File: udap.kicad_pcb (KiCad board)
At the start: 2 copper layers, 25 x 10 mm, 25 parts, among them J201 Conn_02x04_Counter_Clockwise, P1 USB_C_Plug, U2 MIC5245-3.3YM5, U201 NUF6401MNT1, U202 STM32F042F6Px, U4 NUF2042XV6T1G

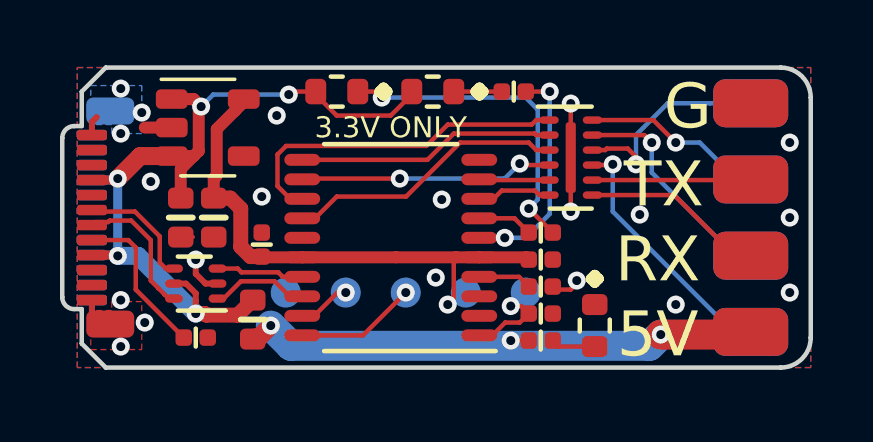
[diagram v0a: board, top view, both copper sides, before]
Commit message: Move the testpoints towards the USB connector
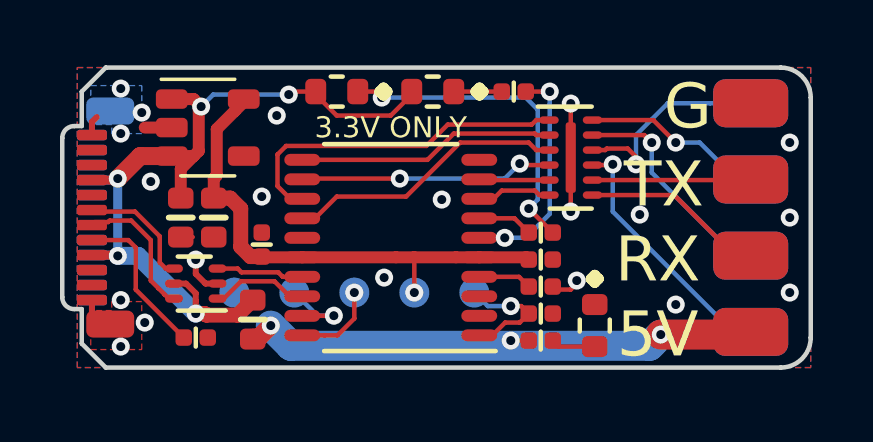
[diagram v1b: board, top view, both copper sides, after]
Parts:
- moved TP1 1.71 mm to (97.3, 108.5)
- moved TP2 1.71 mm to (99.3, 108.5)
- moved TP201 1.71 mm to (101.3, 108.5)
- moved TP202 1.71 mm to (103.3, 108.5)
- moved TP3 1.71 mm to (95.3, 108.5)
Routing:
- net /core/SWDIO: track 1.77 -> 3.09 mm
- net /core/SWCLK: track 4.04 -> 2.83 mm
- net +3V3: track 18.2 -> 17.0 mm
- net /core/BOOT0: track 3.77 -> 4.53 mm
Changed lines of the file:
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@@
     (thickness 0.7)
     (drawings 30)
-    (tracks 262)
+    (tracks 265)
     (zones 0)
     (modules 25)
@@
   (setup
     (last_trace_width 0.15)
+    (user_trace_width 0.15)
+    (user_trace_width 0.6)
     (trace_clearance 0.15)
     (zone_clearance 0.15)
@@
   )
   (module TestPoint:TestPoint_Pad_D1.0mm (layer B.Cu)
-    (at 105 108.5)
+    (at 103.2855 108.5)
     (descr "SMD pad as test Point, diameter 1.0mm")
     (tags "test point SMD pad")
@@
   )
   (module TestPoint:TestPoint_Pad_D1.0mm (layer B.Cu)
-    (at 103 108.5)
+    (at 101.2855 108.5)
     (descr "SMD pad as test Point, diameter 1.0mm")
     (tags "test point SMD pad")
@@
   )
   (module TestPoint:TestPoint_Pad_D1.0mm (layer B.Cu)
-    (at 97 108.5)
+    (at 95.2855 108.5)
     (descr "SMD pad as test Point, diameter 1.0mm")
     (tags "test point SMD pad")
@@
   )
   (module TestPoint:TestPoint_Pad_D1.0mm (layer B.Cu)
-    (at 101 108.5)
+    (at 99.2855 108.5)
     (descr "SMD pad as test Point, diameter 1.0mm")
     (tags "test point SMD pad")
@@
   )
   (module TestPoint:TestPoint_Pad_D1.0mm (layer B.Cu)
-    (at 99 108.5)
+    (at 97.2855 108.5)
     (descr "SMD pad as test Point, diameter 1.0mm")
     (tags "test point SMD pad")
@@
     )
   )
-  (gr_text BT0 (at 105 110) (layer B.SilkS)
+  (gr_text BT0 (at 103.2855 110) (layer B.SilkS)
     (effects (font (size 0.7 0.7) (thickness 0.15)) (justify mirror))
   )
@@
     (effects (font (size 1.5 1.5) (thickness 0.35)) (justify mirror))
   )
-  (gr_text CK (at 101 110) (layer B.SilkS)
+  (gr_text CK (at 99.2855 110) (layer B.SilkS)
     (effects (font (size 0.7 0.7) (thickness 0.15)) (justify mirror))
   )
-  (gr_text IO (at 99 110) (layer B.SilkS)
+  (gr_text IO (at 97.2855 110) (layer B.SilkS)
     (effects (font (size 0.7 0.7) (thickness 0.15)) (justify mirror))
   )
-  (gr_text GND (at 97 110) (layer B.SilkS)
+  (gr_text GND (at 95.2855 110) (layer B.SilkS)
     (effects (font (size 0.7 0.7) (thickness 0.15)) (justify mirror))
   )
-  (gr_text 3V (at 103 110) (layer B.SilkS)
+  (gr_text 3V (at 101.2855 110) (layer B.SilkS)
     (effects (font (size 0.7 0.7) (thickness 0.15)) (justify mirror))
   )
@@
   (segment (start 97.55 107.325) (end 96.275 107.325) (width 0.4) (layer F.Cu) (net 1))
   (segment (start 97.55 107.325) (end 100.675 107.325) (width 0.4) (layer F.Cu) (net 1))
-  (segment (start 100.675 107.325) (end 102.675 107.325) (width 0.4) (layer F.Cu) (net 1))
   (segment (start 102.675 107.325) (end 103.45 107.325) (width 0.4) (layer F.Cu) (net 1))
-  (via (at 102.4 108.9) (size 0.6) (drill 0.3) (layers F.Cu B.Cu) (net 1))
-  (segment (start 102.600037 108.699963) (end 102.4 108.9) (width 0.15) (layer F.Cu) (net 1))
+  (via (at 101.2855 108.5) (size 0.6) (drill 0.3) (layers F.Cu B.Cu) (net 1))
   (segment (start 102.675 107.325) (end 102.600037 107.399963) (width 0.15) (layer F.Cu) (net 1))
-  (segment (start 102.600037 107.399963) (end 102.600037 108.699963) (width 0.15) (layer F.Cu) (net 1))
-  (segment (start 102.8 108.5) (end 102.4 108.9) (width 0.15) (layer B.Cu) (net 1))
-  (segment (start 103 108.5) (end 102.8 108.5) (width 0.15) (layer B.Cu) (net 1))
   (segment (start 105.025 107.325) (end 105.1 107.4) (width 0.4) (layer F.Cu) (net 1))
   (segment (start 103.45 107.325) (end 105.025 107.325) (width 0.4) (layer F.Cu) (net 1))
@@
   (segment (start 95.5 105.7) (end 95.5 106.975) (width 0.5) (layer F.Cu) (net 1))
   (segment (start 95.15 105.35) (end 95.5 105.7) (width 0.5) (layer F.Cu) (net 1))
+  (segment (start 101.2855 107.3307) (end 101.2798 107.325) (width 0.15) (layer F.Cu) (net 1))
+  (segment (start 101.2855 108.5) (end 101.2855 107.3307) (width 0.15) (layer F.Cu) (net 1))
+  (segment (start 100.675 107.325) (end 101.2798 107.325) (width 0.4) (layer F.Cu) (net 1))
+  (segment (start 101.2798 107.325) (end 102.675 107.325) (width 0.4) (layer F.Cu) (net 1))
   (via (at 91.5 101.7) (size 0.6) (drill 0.3) (layers F.Cu B.Cu) (net 2))
   (via (at 91.5 108.75) (size 0.6) (drill 0.3) (layers F.Cu B.Cu) (net 2))
@@
   (via (at 102.2 105.4) (size 0.6) (drill 0.3) (layers F.Cu B.Cu) (net 2))
   (via (at 92.5 104.8) (size 0.6) (drill 0.3) (layers F.Cu B.Cu) (net 2))
-  (via (at 102 108) (size 0.6) (drill 0.3) (layers F.Cu B.Cu) (net 2))
+  (via (at 100.2792 108.0008) (size 0.6) (drill 0.3) (layers F.Cu B.Cu) (net 2))
   (via (at 110 108.9) (size 0.6) (drill 0.3) (layers F.Cu B.Cu) (net 2))
   (segment (start 106.7 108.2) (end 106.7 108.1) (width 0.15) (layer F.Cu) (net 2))
@@
   (segment (start 93.3 103) (end 92.3 103) (width 0.4) (layer F.Cu) (net 2))
   (via (at 96.2 105.3) (size 0.6) (drill 0.3) (layers F.Cu B.Cu) (net 2))
+  (segment (start 107.1 108.9) (end 107.3 108.9) (width 0.15) (layer F.Cu) (net 2))
   (via (at 91.4 104.7) (size 0.6) (drill 0.3) (layers F.Cu B.Cu) (net 3))
   (segment (start 90.54 104.75) (end 91.35 104.75) (width 0.3) (layer F.Cu) (net 3))
@@
   (segment (start 104.85 108.95) (end 105.1 109.2) (width 0.15) (layer F.Cu) (net 9))
   (segment (start 104.5 108.95) (end 104.85 108.95) (width 0.15) (layer F.Cu) (net 9))
-  (segment (start 104.55 108.95) (end 105 108.5) (width 0.15) (layer B.Cu) (net 9))
   (segment (start 104.5 108.95) (end 104.55 108.95) (width 0.15) (layer B.Cu) (net 9))
-  (via (at 101.000026 108.5) (size 0.6) (drill 0.3) (layers F.Cu B.Cu) (net 10))
-  (segment (start 97.55 109.925) (end 99.575026 109.925) (width 0.15) (layer F.Cu) (net 10))
-  (segment (start 100.700027 108.799999) (end 101.000026 108.5) (width 0.15) (layer F.Cu) (net 10))
-  (segment (start 99.575026 109.925) (end 100.700027 108.799999) (width 0.15) (layer F.Cu) (net 10))
-  (via (at 98.99997 108.5) (size 0.6) (drill 0.3) (layers F.Cu B.Cu) (net 11))
-  (segment (start 98.725 108.5) (end 98.99997 108.5) (width 0.15) (layer F.Cu) (net 11))
-  (segment (start 97.95 109.275) (end 98.725 108.5) (width 0.15) (layer F.Cu) (net 11))
+  (segment (start 103.7355 108.95) (end 103.2855 108.5) (width 0.15) (layer B.Cu) (net 9))
+  (segment (start 104.5 108.95) (end 103.7355 108.95) (width 0.15) (layer B.Cu) (net 9))
+  (via (at 99.2855 108.5) (size 0.6) (drill 0.3) (layers F.Cu B.Cu) (net 10))
+  (segment (start 98.3 109.925) (end 97.55 109.925) (width 0.15) (layer F.Cu) (net 10))
+  (segment (start 98.725602 109.925) (end 98.3 109.925) (width 0.15) (layer F.Cu) (net 10))
+  (segment (start 99.2855 109.365102) (end 98.725602 109.925) (width 0.15) (layer F.Cu) (net 10))
+  (segment (start 99.2855 108.5) (end 99.2855 109.365102) (width 0.15) (layer F.Cu) (net 10))
+  (via (at 98.6028 109.2708) (size 0.6) (drill 0.3) (layers F.Cu B.Cu) (net 11))
   (segment (start 97.55 109.275) (end 97.95 109.275) (width 0.15) (layer F.Cu) (net 11))
+  (segment (start 98.5986 109.275) (end 98.6028 109.2708) (width 0.15) (layer F.Cu) (net 11))
+  (segment (start 97.55 109.275) (end 98.5986 109.275) (width 0.15) (layer F.Cu) (net 11))
+  (segment (start 98.0563 109.2708) (end 97.2855 108.5) (width 0.15) (layer B.Cu) (net 11))
+  (segment (start 98.6028 109.2708) (end 98.0563 109.2708) (width 0.15) (layer B.Cu) (net 11))
   (segment (start 95.4 107.7) (end 94.725 107.7) (width 0.15) (layer F.Cu) (net 12))
   (segment (start 96.749286 107.825008) (end 95.525008 107.825008) (width 0.15) (layer F.Cu) (net 12))
@@
   (segment (start 104.775 107.975) (end 105.1 108.3) (width 0.15) (layer F.Cu) (net 13))
   (segment (start 103.45 107.975) (end 104.775 107.975) (width 0.15) (layer F.Cu) (net 13))
-  (segment (start 107.1 108.9) (end 107.3 108.9) (width 0.15) (layer F.Cu) (net 2))
   (segment (start 106.1 110.3) (end 105.9 110.1) (width 0.15) (layer F.Cu) (net 14))
   (segment (start 107.3 110.3) (end 106.1 110.3) (width 0.15) (layer F.Cu) (net 14))
